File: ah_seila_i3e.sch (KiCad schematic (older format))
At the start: 5 parts, among them Q4 BC548

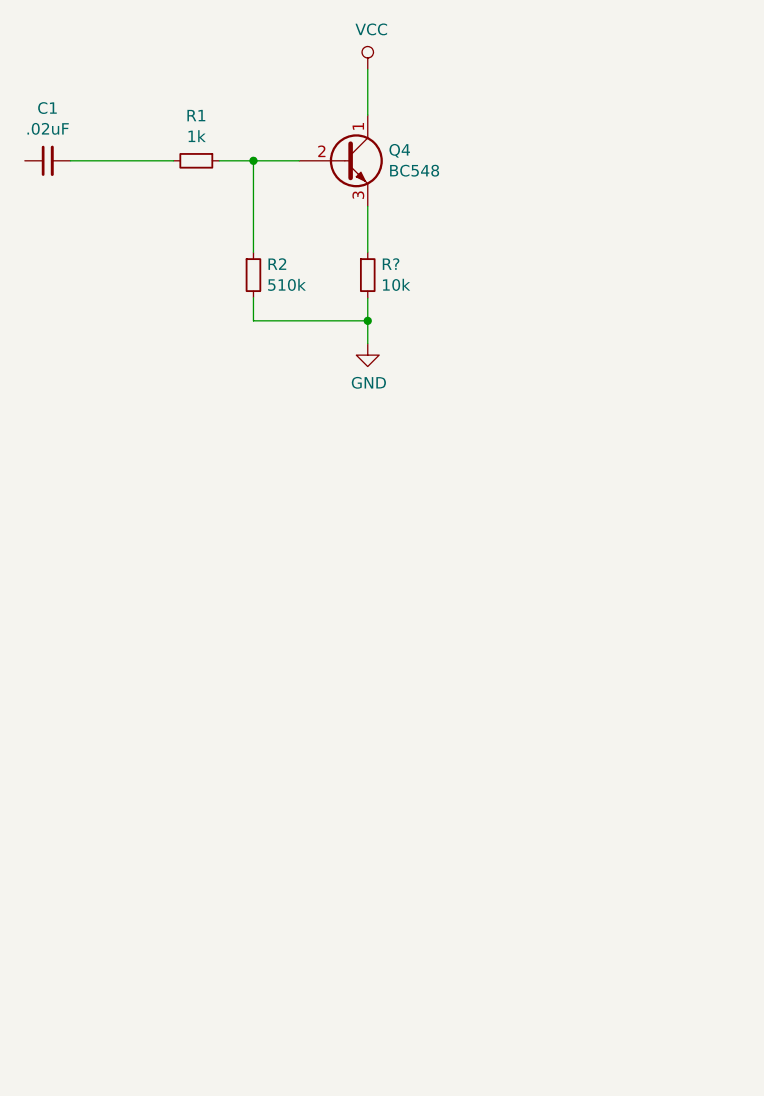
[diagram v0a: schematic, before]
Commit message: footprints selecionadas
selecionados os encapsulamentos
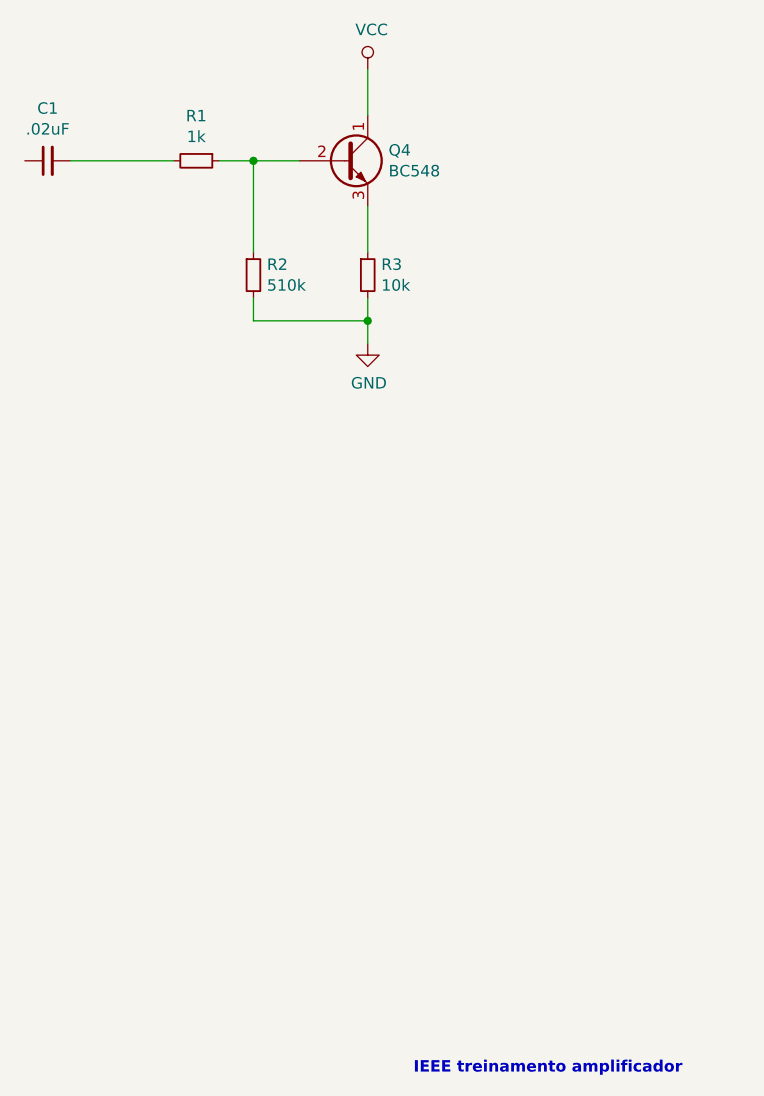
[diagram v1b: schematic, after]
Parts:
- C1: footprint (none) -> Capacitor_THT:C_Disc_D3.0mm_W2.0mm_P2.50mm
- R1, R2: footprint (none) -> Resistor_THT:R_Axial_DIN0207_L6.3mm_D2.5mm_P7.62mm_Horizontal
- R3: renamed from R?; footprint (none) -> Resistor_THT:R_Axial_DIN0207_L6.3mm_D2.5mm_P7.62mm_Horizontal
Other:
- note added: "IEEE treinamento amplificador"
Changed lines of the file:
@@
 F 0 "R2" H 6709 4046 50  0000 L CNN
 F 1 "510k" H 6709 3955 50  0000 L CNN
-F 2 "" H 6650 4000 50  0001 C CNN
+F 2 "Resistor_THT:R_Axial_DIN0207_L6.3mm_D2.5mm_P7.62mm_Horizontal" H 6650 4000 50  0001 C CNN
 F 3 "~" H 6650 4000 50  0001 C CNN
 	1    6650 4000
@@
 F 0 "R1" V 6204 3500 50  0000 C CNN
 F 1 "1k" V 6295 3500 50  0000 C CNN
-F 2 "" H 6400 3500 50  0001 C CNN
+F 2 "Resistor_THT:R_Axial_DIN0207_L6.3mm_D2.5mm_P7.62mm_Horizontal" H 6400 3500 50  0001 C CNN
 F 3 "~" H 6400 3500 50  0001 C CNN
 	1    6400 3500
@@
 $EndComp
 $Comp
-L Device:R_Small R?
+L Device:R_Small R3
 U 1 1 5D4E5023
 P 7150 4000
-F 0 "R?" H 7209 4046 50  0000 L CNN
+F 0 "R3" H 7209 4046 50  0000 L CNN
 F 1 "10k" H 7209 3955 50  0000 L CNN
-F 2 "" H 7150 4000 50  0001 C CNN
+F 2 "Resistor_THT:R_Axial_DIN0207_L6.3mm_D2.5mm_P7.62mm_Horizontal" H 7150 4000 50  0001 C CNN
 F 3 "~" H 7150 4000 50  0001 C CNN
 	1    7150 4000
@@
 $EndComp
 $Comp
-L power:GND #PWR?
+L power:GND #PWR0101
 U 1 1 5D4EA839
 P 7150 4300
-F 0 "#PWR?" H 7150 4050 50  0001 C CNN
+F 0 "#PWR0101" H 7150 4050 50  0001 C CNN
 F 1 "GND" H 7155 4127 50  0000 C CNN
 F 2 "" H 7150 4300 50  0001 C CNN
@@
 $EndComp
 $Comp
-L power:VCC #PWR?
+L power:VCC #PWR0102
 U 1 1 5D4EB24B
 P 7150 3100
-F 0 "#PWR?" H 7150 2950 50  0001 C CNN
+F 0 "#PWR0102" H 7150 2950 50  0001 C CNN
 F 1 "VCC" H 7167 3273 50  0000 C CNN
 F 2 "" H 7150 3100 50  0001 C CNN
@@
 F 0 "C1" V 5979 3500 50  0000 C CNN
 F 1 ".02uF" V 5888 3500 50  0000 C CNN
-F 2 "" H 5750 3500 50  0001 C CNN
+F 2 "Capacitor_THT:C_Disc_D3.0mm_W2.0mm_P2.50mm" H 5750 3500 50  0001 C CNN
 F 3 "~" H 5750 3500 50  0001 C CNN
 	1    5750 3500
@@
 Wire Wire Line
 	7150 4200 7150 4300
+Text Notes 7350 7500 0    50   ~ 10
+IEEE treinamento amplificador
 $EndSCHEMATC
